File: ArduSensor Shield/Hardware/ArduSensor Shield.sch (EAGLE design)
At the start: 23 parts

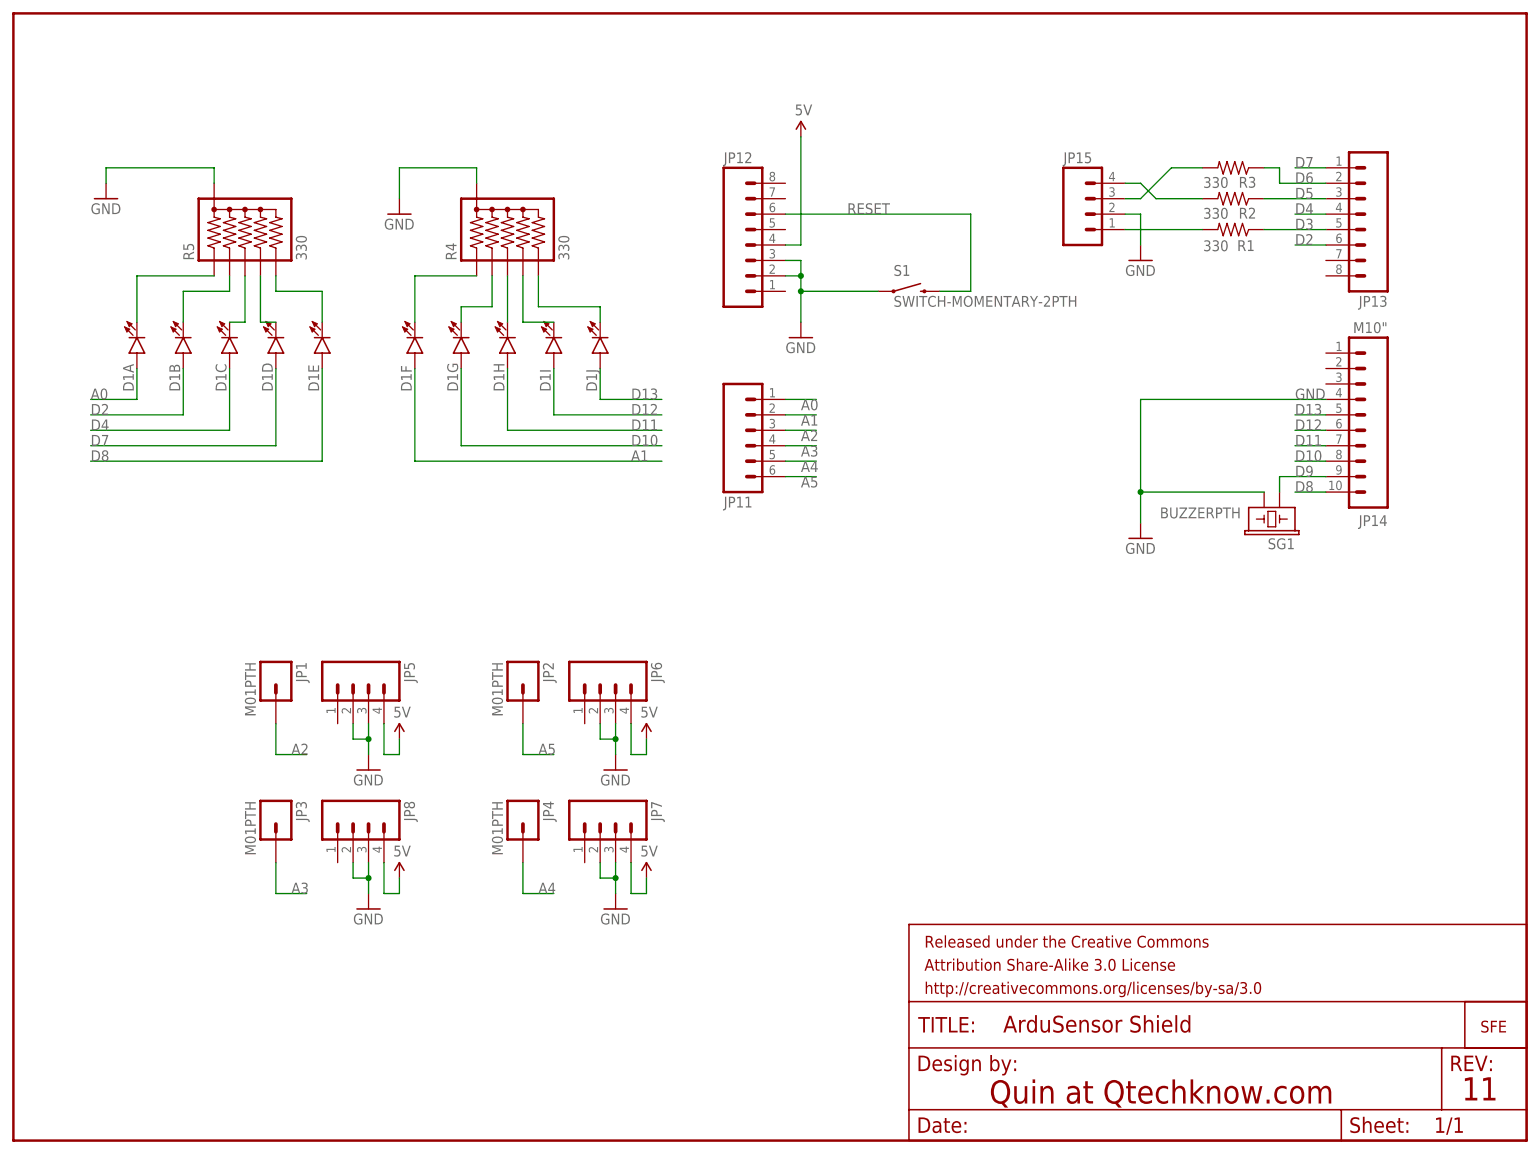
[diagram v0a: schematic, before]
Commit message: Adding Shield hardware version 1.2
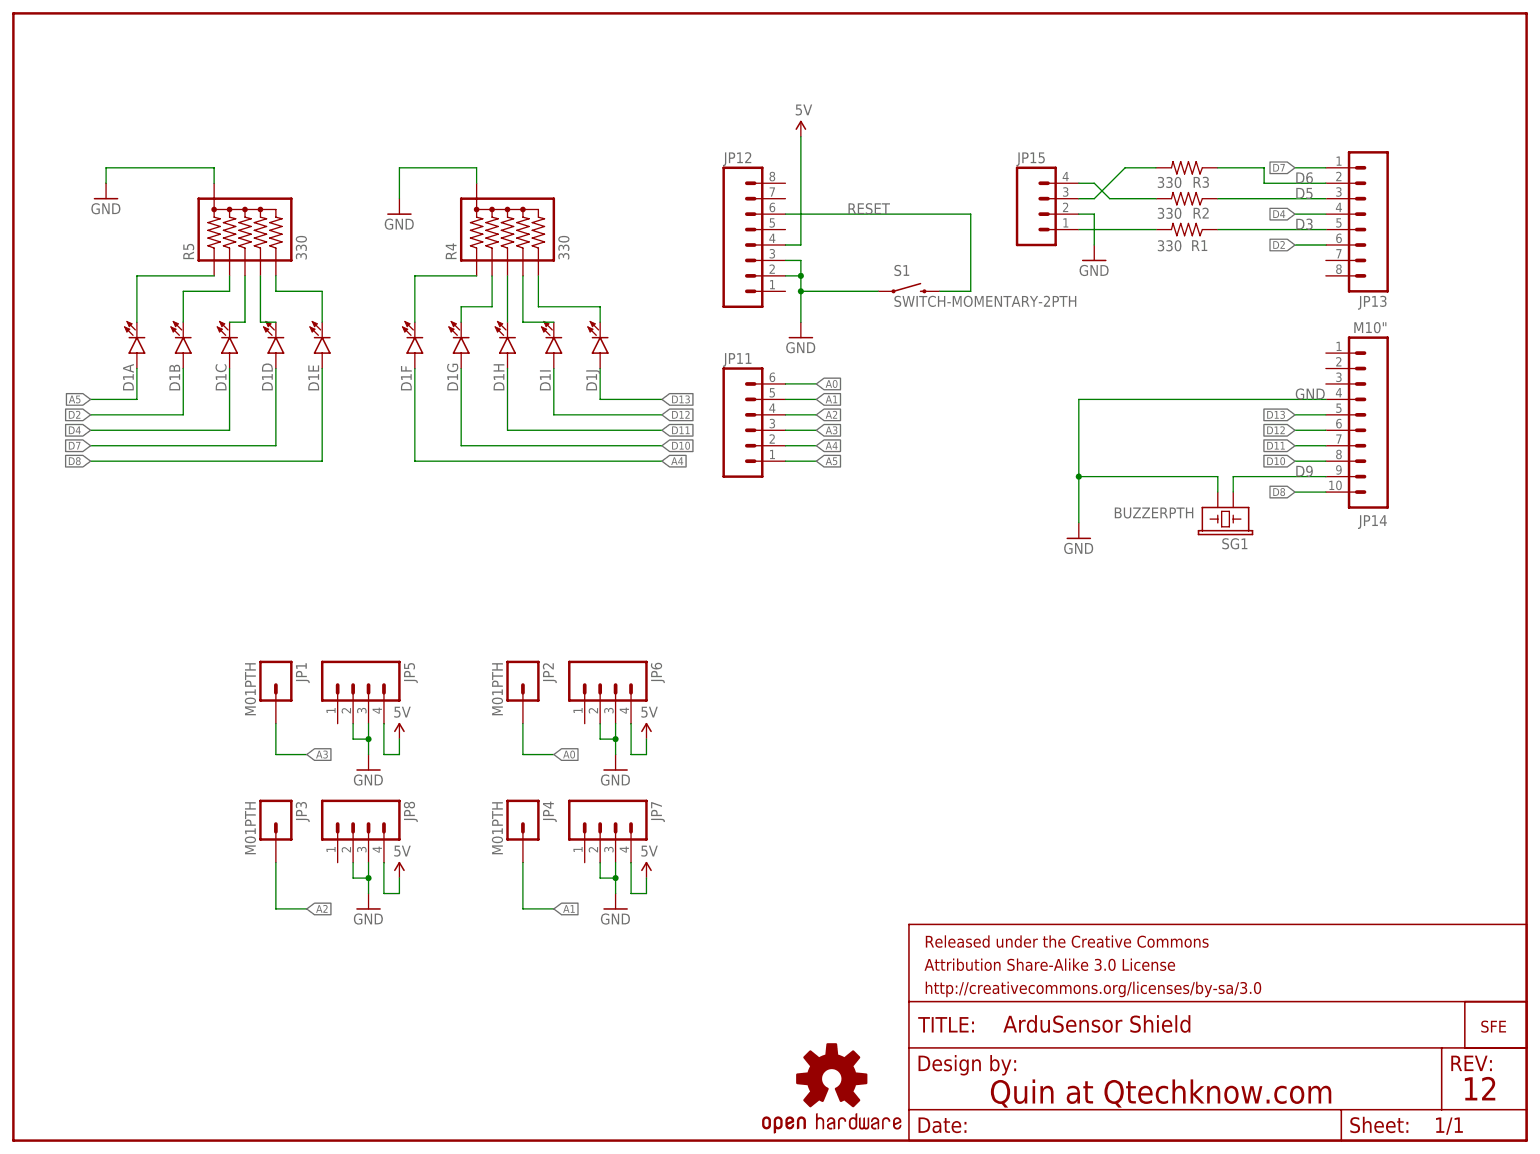
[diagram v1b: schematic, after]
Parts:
- added LOGO1: OSHW-LOGOM, SparkFun-Aesthetics:OSHW-LOGOM
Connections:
- net A0: now also JP11.6, JP2.1; no longer D1A.A, JP11.1
- net A1: now also JP11.5, JP4.1; no longer D1F.A, JP11.2
- net A2: now also JP11.4, JP3.1; no longer JP1.1, JP11.3
- net A3: now also JP1.1, JP11.3; no longer JP11.4, JP3.1
- net A4: now also D1F.A, JP11.2; no longer JP11.5, JP4.1
- net A5: now also D1A.A, JP11.1; no longer JP11.6, JP2.1
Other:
- note added: "12"
- note removed: "11"
- moved on the sheet: JP11, JP15, R1, R2, R3, SG1
